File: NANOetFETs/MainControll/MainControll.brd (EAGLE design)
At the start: 85 x 55 mm, 18 parts

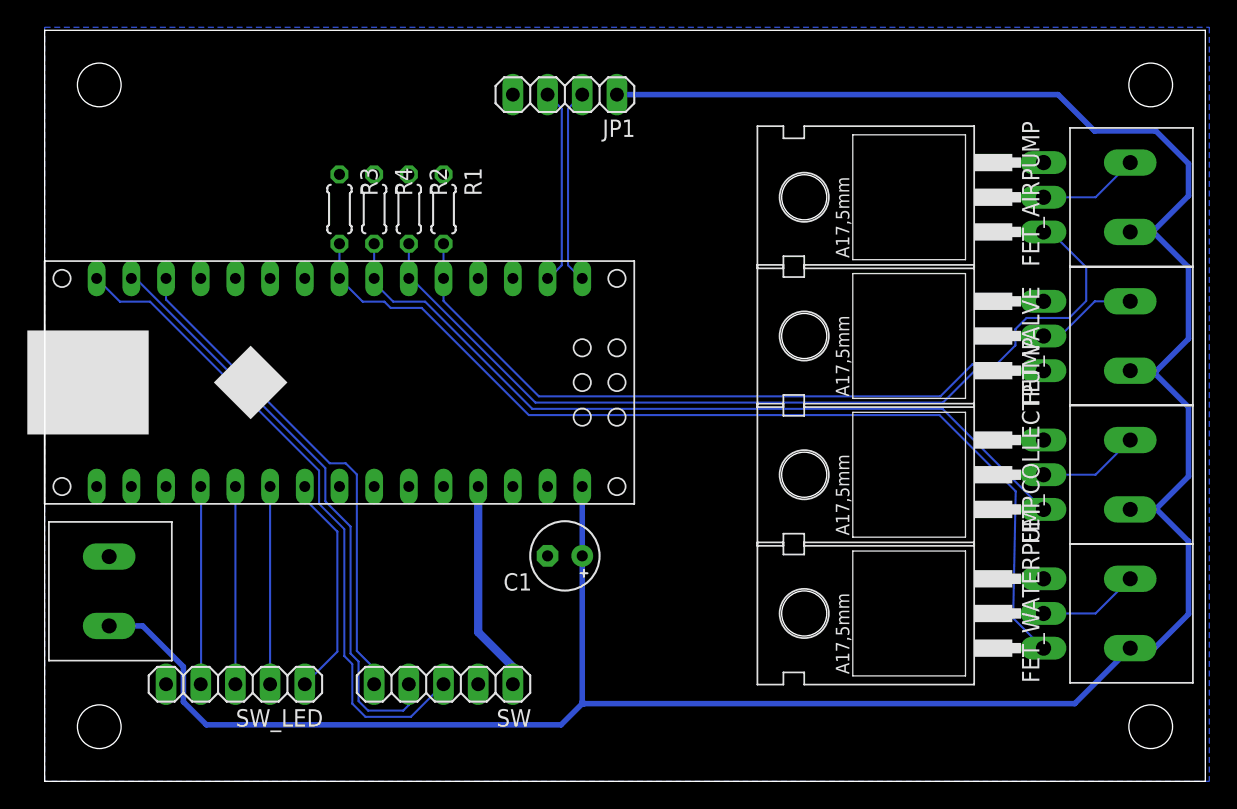
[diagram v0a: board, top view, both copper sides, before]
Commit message: Modifed wire thinkness bolder; Rerouted as well;
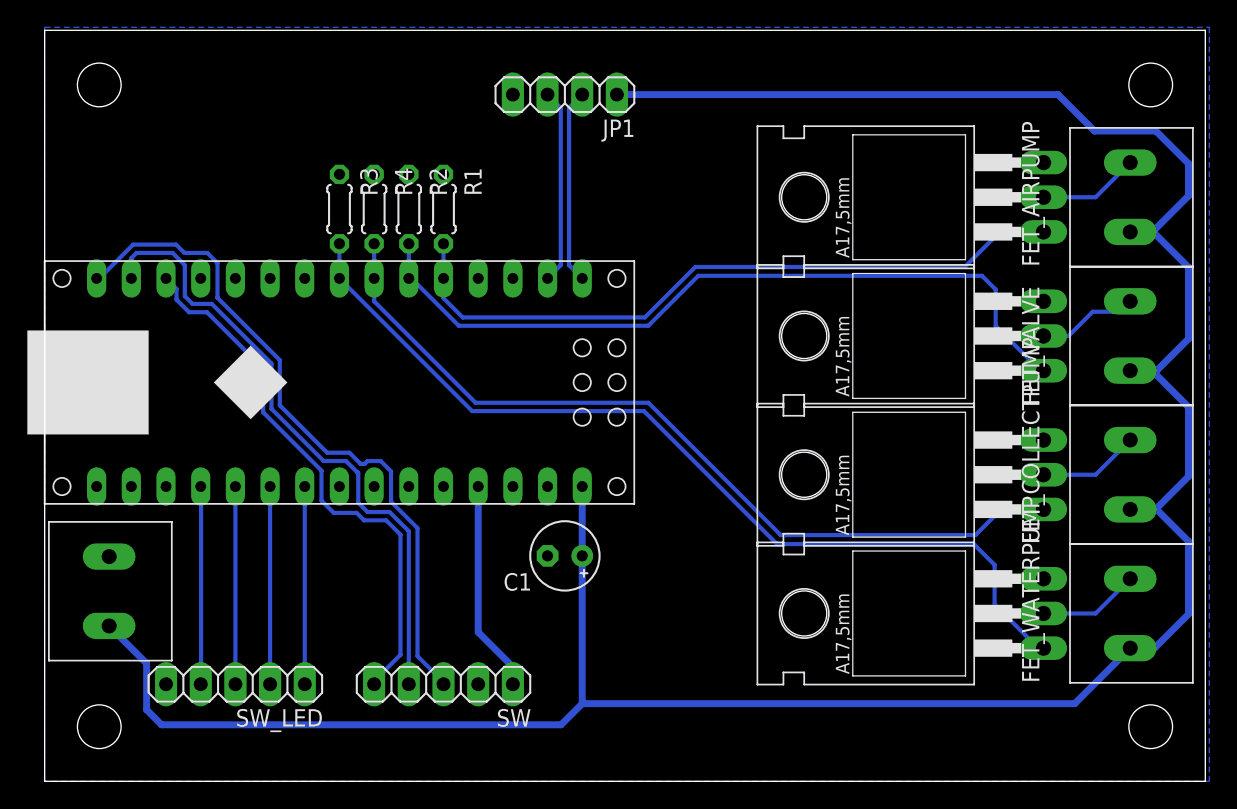
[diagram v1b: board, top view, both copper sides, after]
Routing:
- net AIRPUMP: track 64.4 -> 51.1 mm
- net WATPUMP: track 71.4 -> 67.4 mm
- net SW1: track 36.7 -> 40.3 mm
- net COLPUMP: track 58.7 -> 61.4 mm
- net VALVE: track 53.8 -> 56.4 mm
- net SW2: track 43.7 -> 46.1 mm
- net SW3: track 48.3 -> 50.3 mm
- net N$14: track 16.5 -> 14.5 mm
